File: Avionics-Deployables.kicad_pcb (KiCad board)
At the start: 2 copper layers, 82.6 x 90 mm, 0 parts

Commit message: Export BOM
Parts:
- added D1: DFLS130L-7, Diode_SMD:D_PowerDI-123, F.Cu at (109.4, 74.5)
- added D10: DFLS130L-7, Diode_SMD:D_PowerDI-123, B.Cu at (109.4, 117.0)
- added D2: DFLS130L-7, Diode_SMD:D_PowerDI-123, F.Cu at (109.4, 117.0)
- added D3: DFLS130L-7, Diode_SMD:D_PowerDI-123, F.Cu at (155.9, 129.8)
- added D4: DFLS130L-7, Diode_SMD:D_PowerDI-123, F.Cu at (185.3, 74.5)
- added D5: DFLS130L-7, Diode_SMD:D_PowerDI-123, F.Cu at (185.3, 117.0)
- added D6: DFLS130L-7, Diode_SMD:D_PowerDI-123, B.Cu at (185.3, 74.5)
- added D7: DFLS130L-7, Diode_SMD:D_PowerDI-123, B.Cu at (185.3, 117.0)
- added D8: DFLS130L-7, Diode_SMD:D_PowerDI-123, B.Cu at (138.7, 129.8)
- added D9: DFLS130L-7, Diode_SMD:D_PowerDI-123, B.Cu at (109.4, 74.5)
- added J1: 200528-0100, Connector_FFC-FPC:Molex_200528-0100_1x10-1MP_P1.00mm_Horizontal, B.Cu at (147.3, 136.2)
- added SC1: SM141K06TF, SolarPanels:SM141K06TF, F.Cu at (123.8, 74.5)
- added SC10: SM141K06TF, SolarPanels:SM141K06TF, B.Cu at (123.8, 117.0)
- added SC2: SM141K06TF, SolarPanels:SM141K06TF, F.Cu at (123.8, 117.0)
- added SC3: SM141K06TF, SolarPanels:SM141K06TF, F.Cu at (147.3, 106.7)
- added SC4: SM141K06TF, SolarPanels:SM141K06TF, F.Cu at (170.8, 74.5)
- added SC5: SM141K06TF, SolarPanels:SM141K06TF, F.Cu at (170.8, 117.0)
- added SC6: SM141K06TF, SolarPanels:SM141K06TF, B.Cu at (170.8, 74.5)
- added SC7: SM141K06TF, SolarPanels:SM141K06TF, B.Cu at (170.8, 117.0)
- added SC8: SM141K06TF, SolarPanels:SM141K06TF, B.Cu at (147.3, 106.7)
- added SC9: SM141K06TF, SolarPanels:SM141K06TF, B.Cu at (123.8, 74.5)
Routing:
- net Net-(D3-K): track 0.00 -> 130.5 mm
- net Net-(D8-K): track 0.00 -> 128.9 mm
- net Net-(D7-K): track 0.00 -> 77.3 mm
- net Net-(D2-K): track 0.00 -> 77.2 mm
- net Net-(D6-K): track 0.00 -> 63.2 mm
- net Net-(D4-K): track 0.00 -> 60.8 mm
- net Net-(D1-K): track 0.00 -> 60.8 mm
- net Net-(D10-A): track 0.00 -> 60.7 mm
- net D_VSOLAR1: track 0.00 -> 59.9 mm, vias 0 -> 3
- net D_VSOLAR2: track 0.00 -> 53.4 mm
- net GND: vias 0 -> 741
- added copper zone on B.Cu, net D_VSOLAR1
- added copper zone on B.Cu, net D_VSOLAR2
- added copper zone on B.Cu, net GND
- added copper zone on F.Cu, net GND
- removed copper zone on B.Cu, net (none)
- removed copper zone on F.Cu, net (none)
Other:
- outline, holes or cut-outs redrawn
- board text added: "1"
- board text added: "10"
- board text added: "ARGUS-1"
- board text added: "DVSOLAR1"
- board text added: "DVSOLAR2"
- board text added: "GND"
- board text added: "TO X/Y SOLAR PANEL"
- board text removed: "Solar Deployables Mechanical Stand-in 0.8mm"

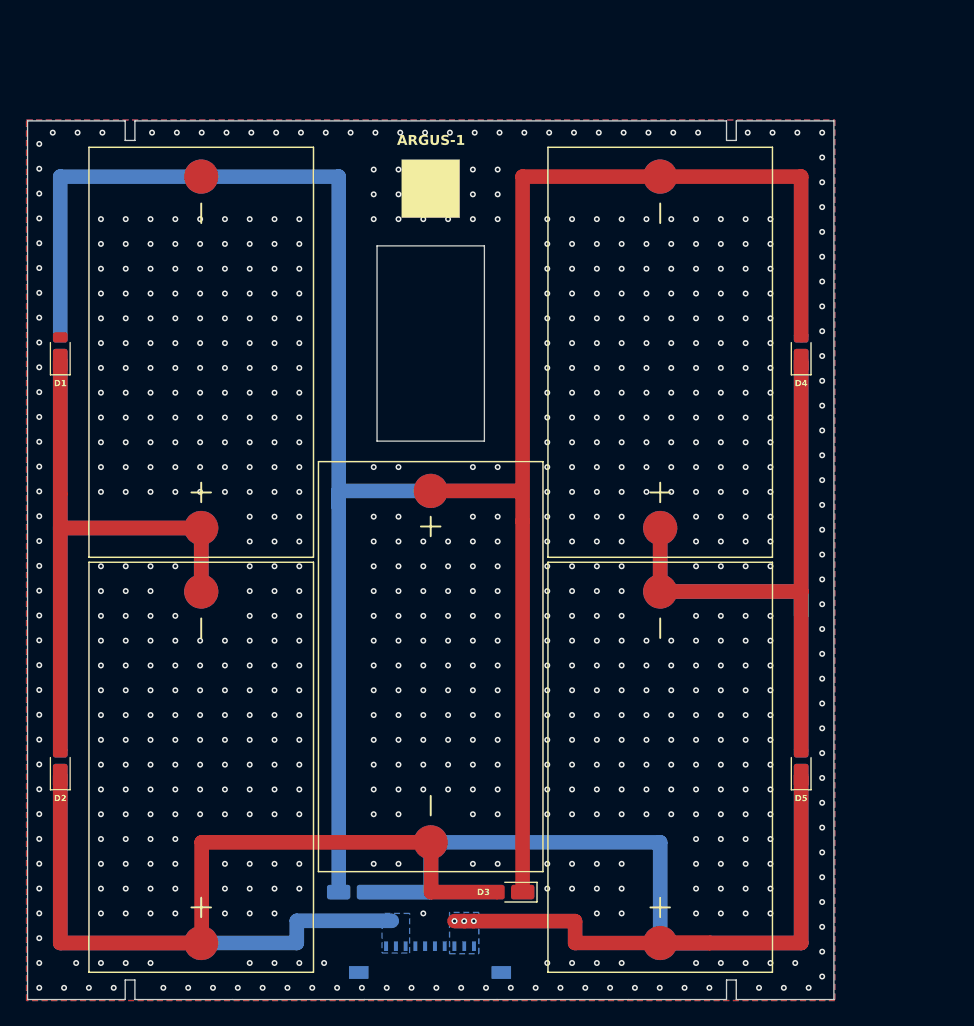
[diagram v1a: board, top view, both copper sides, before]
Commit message: Update Deployable outlines
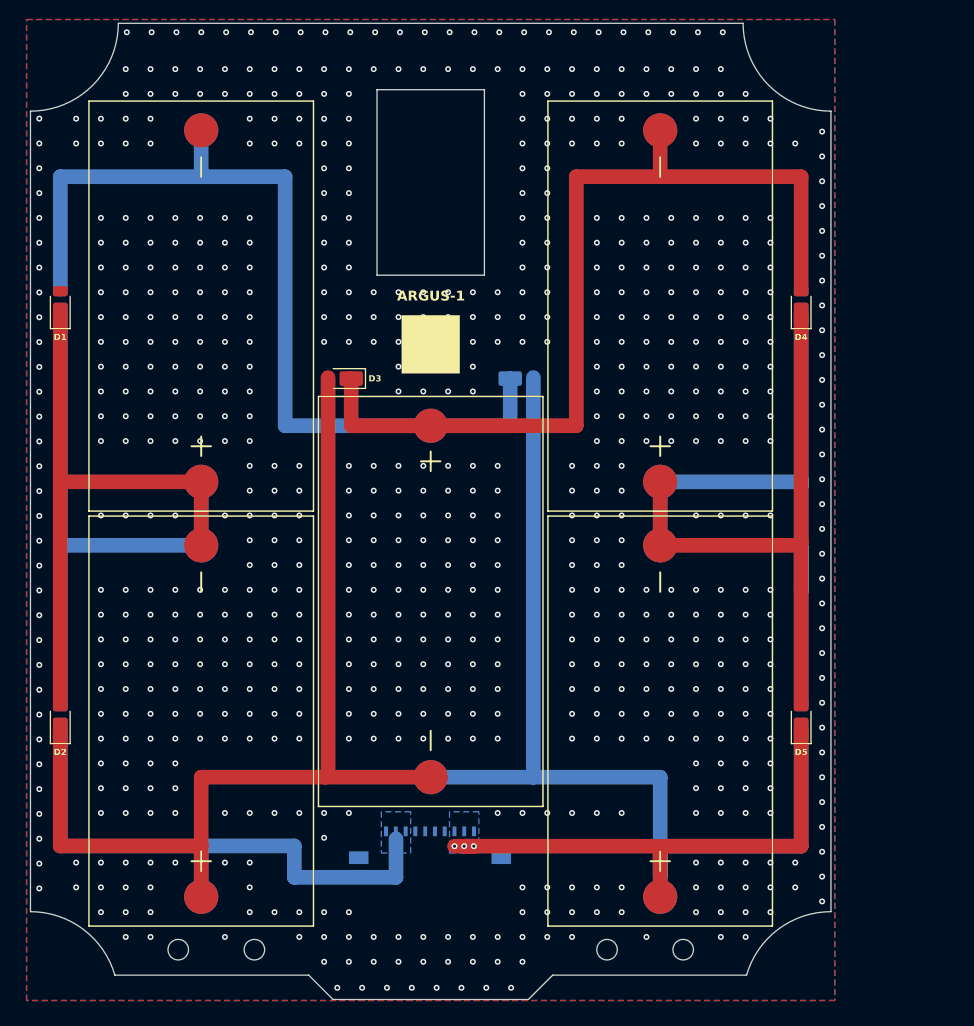
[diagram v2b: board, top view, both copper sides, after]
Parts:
- moved D3 55.5 mm to (138.3, 77.2)
- moved D8 55.5 mm to (156.3, 77.2)
- moved J1 11.8 mm to (147.3, 124.5)
- moved SC3 6.67 mm to (147.3, 100.0)
- moved SC8 6.67 mm to (147.3, 100.0)
- moved D10 4.73 mm to (109.4, 112.3)
- moved D2 4.73 mm to (109.4, 112.3)
- moved D5 4.73 mm to (185.3, 112.3)
- moved D7 4.73 mm to (185.3, 112.3)
- moved SC10 4.73 mm to (123.8, 112.3)
- moved SC2 4.73 mm to (123.8, 112.3)
- moved SC5 4.73 mm to (170.8, 112.3)
- moved SC7 4.73 mm to (170.8, 112.3)
- moved D1 4.73 mm to (109.4, 69.7)
- moved D4 4.73 mm to (185.3, 69.7)
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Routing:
- net Net-(D3-K): track 130.5 -> 92.7 mm
- net Net-(D8-K): track 128.9 -> 92.8 mm
- net Net-(D7-K): track 77.3 -> 106.2 mm
- net Net-(D2-K): track 77.2 -> 103.2 mm
- net D_VSOLAR1: track 59.9 -> 53.6 mm
- net D_VSOLAR2: track 53.4 -> 58.7 mm
- net Net-(D6-K): track 63.2 -> 66.2 mm
- net GND: vias 741 -> 744
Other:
- board size 82.6 x 90 mm -> 82 x 100 mm

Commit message: Update solar cell footprints
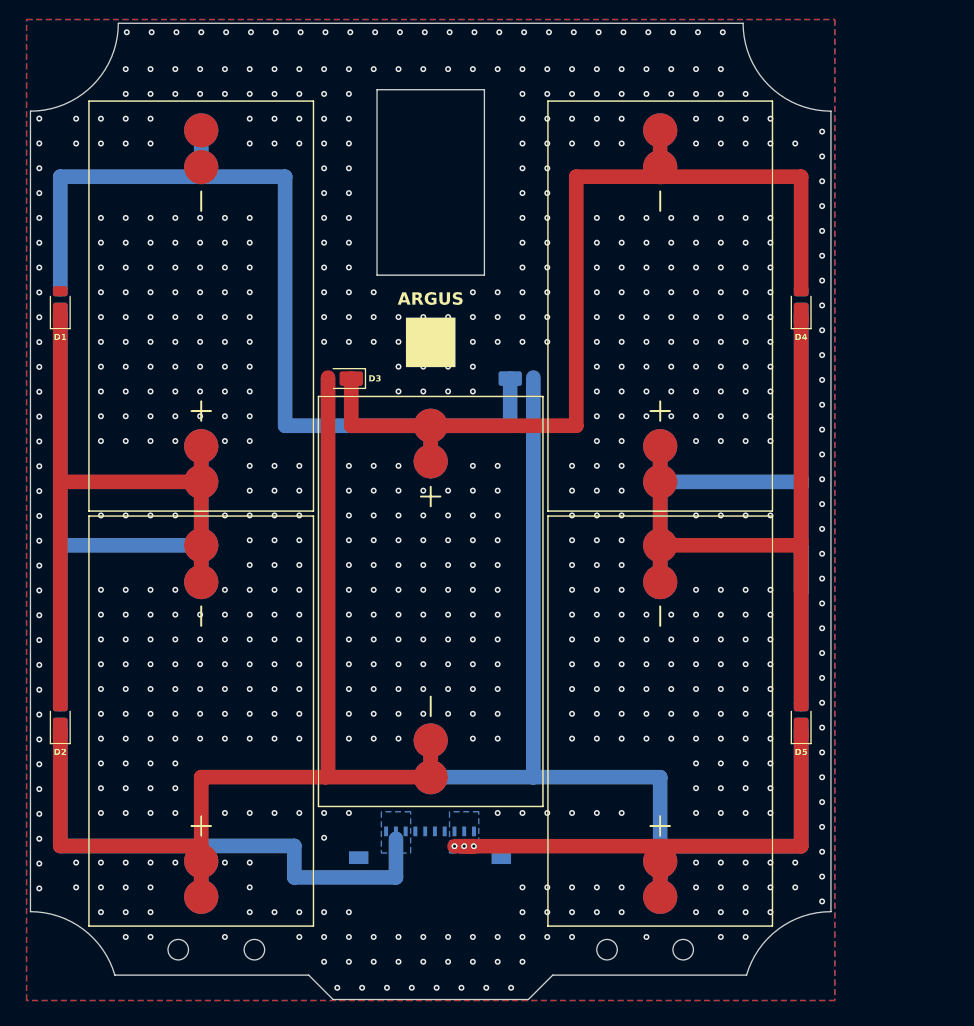
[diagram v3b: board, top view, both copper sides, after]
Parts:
- SC1, SC10, SC2, SC3, SC4, SC5, SC6, SC7, SC8, SC9: footprint SolarPanels:SM141K06TF -> SolarPanels:SM141K06TF-S
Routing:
- net Net-(D10-A): track 61.0 -> 68.4 mm
- net Net-(D4-K): track 61.0 -> 68.4 mm
- net Net-(D6-K): track 66.2 -> 73.6 mm
- net Net-(D1-K): track 60.9 -> 67.1 mm
- net Net-(D7-K): track 106.2 -> 109.9 mm
- net Net-(D2-K): track 103.2 -> 107.0 mm
- net Net-(D8-K): track 92.8 -> 96.4 mm
- net Net-(D3-K): track 92.7 -> 96.3 mm
- net GND: vias 744 -> 731
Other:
- board text added: "ARGUS"
- board text removed: "ARGUS-1"

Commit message: v2.3 Updates
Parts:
- added ?: , clipboard:eb50a26b-5fb6-463a-8dd0-ee5887daaa13, F.Cu at (142.4, 69.8)
- added ?: , clipboard:eb50a26b-5fb6-463a-8dd0-ee5887daaa13, B.Cu at (150.7, 69.8)
- added REF**: X Label, X Label, F.Cu at (146.6, 72.8)
- added REF**: X Label, X Label, B.Cu at (146.6, 72.8)
- added Ref**: Val**, custom-footprints:ypanel, F.Cu at (198.6, 73.1)
- added Ref**: Val**, custom-footprints:ypanel, B.Cu at (198.6, 73.1)
- SC1, SC10, SC2, SC3, SC4, SC5, SC6, SC7, SC8, SC9: value SM141K06TF -> SM141K06TF/S
- moved SC3 3.20 mm to (146.7, 103.1)
- moved SC8 3.20 mm to (146.7, 103.1)
- moved J1 1.76 mm to (146.6, 126.1)
- moved D3 1.71 mm to (136.9, 78.0), turned to 90 degrees
- moved D1 0.91 mm to (108.7, 70.4)
- moved D10 0.91 mm to (108.7, 112.9)
- moved D2 0.91 mm to (108.7, 112.9)
- moved D9 0.91 mm to (108.7, 70.4)
- moved D4 0.91 mm to (184.6, 70.4)
- moved D5 0.91 mm to (184.6, 112.9)
- moved D6 0.91 mm to (184.6, 70.4)
- moved D7 0.91 mm to (184.6, 112.9)
- moved SC1 0.91 mm to (123.2, 70.4)
- moved SC10 0.91 mm to (123.2, 112.9)
- moved SC2 0.91 mm to (123.2, 112.9)
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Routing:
- net D_VSOLAR2: track 58.7 -> 50.9 mm
- net Net-(D7-K): track 109.9 -> 115.8 mm
- net Net-(D8-K): track 96.4 -> 102.0 mm
- net Net-(D3-K): track 96.3 -> 101.9 mm
- net Net-(D2-K): track 107.0 -> 111.8 mm
- net D_VSOLAR1: track 53.6 -> 51.5 mm
- net GND: vias 731 -> 693
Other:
- outline, holes or cut-outs redrawn
- board text added: "ARGUS CUBESAT"
- board text removed: "ARGUS"

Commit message: V3 Updates and Cell Backer
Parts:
- added H1: MountingHole_Pad, TestPoint:TestPoint_Pad_D1.0mm, F.Cu at (109.6, 84.6)
- added H10: MountingHole_Pad, TestPoint:TestPoint_Pad_D1.0mm, B.Cu at (183.6, 84.6)
- added H11: MountingHole_Pad, TestPoint:TestPoint_Pad_D1.0mm, B.Cu at (183.6, 126.6)
- added H12: MountingHole_Pad, TestPoint:TestPoint_Pad_D1.0mm, B.Cu at (109.6, 56.6)
- added H13: MountingHole_Pad, TestPoint:TestPoint_Pad_D1.0mm, B.Cu at (109.6, 84.6)
- added H14: MountingHole_Pad, TestPoint:TestPoint_Pad_D1.0mm, B.Cu at (109.6, 126.6)
- added H15: MountingHole_Pad, TestPoint:TestPoint_Pad_D1.0mm, B.Cu at (183.6, 98.6)
- added H16: MountingHole_Pad, TestPoint:TestPoint_Pad_D1.0mm, B.Cu at (109.6, 98.6)
- added H17: MountingHole_Pad, TestPoint:TestPoint_Pad_D1.0mm, B.Cu at (183.6, 91.6)
- added H18: MountingHole_Pad, TestPoint:TestPoint_Pad_D1.0mm, B.Cu at (109.6, 91.6)
- added H19: MountingHole_Pad, TestPoint:TestPoint_Pad_D1.0mm, F.Cu at (183.6, 91.6)
- added H2: MountingHole_Pad, TestPoint:TestPoint_Pad_D1.0mm, F.Cu at (183.6, 84.6)
- added H20: MountingHole_Pad, TestPoint:TestPoint_Pad_D1.0mm, F.Cu at (109.6, 91.6)
- added H3: MountingHole_Pad, TestPoint:TestPoint_Pad_D1.0mm, F.Cu at (109.6, 56.6)
- added H4: MountingHole_Pad, TestPoint:TestPoint_Pad_D1.0mm, F.Cu at (109.6, 98.6)
- added H5: MountingHole_Pad, TestPoint:TestPoint_Pad_D1.0mm, F.Cu at (109.6, 126.6)
- added H6: MountingHole_Pad, TestPoint:TestPoint_Pad_D1.0mm, F.Cu at (183.6, 56.6)
- added H7: MountingHole_Pad, TestPoint:TestPoint_Pad_D1.0mm, F.Cu at (183.6, 98.6)
- added H8: MountingHole_Pad, TestPoint:TestPoint_Pad_D1.0mm, F.Cu at (183.6, 126.6)
- added H9: MountingHole_Pad, TestPoint:TestPoint_Pad_D1.0mm, B.Cu at (183.6, 56.6)
- D1, D10, D2, D3, D4, D5, D6, D7, D8, D9: value DFLS130L-7 -> DFLS130LQ-7
- SC1, SC10, SC2, SC3, SC4, SC5, SC6, SC7, SC8, SC9: footprint SolarPanels:SM141K06TF-S -> Argus-Miscellaneous:SM141K06TF_S
- moved D5 1.04 mm to (183.6, 112.6)
- moved D7 1.04 mm to (183.6, 112.6)
- moved D4 1.04 mm to (183.6, 70.6)
- moved D6 1.04 mm to (183.6, 70.6)
- moved D10 0.93 mm to (109.6, 112.6)
- moved D2 0.93 mm to (109.6, 112.6)
- moved D1 0.92 mm to (109.6, 70.6)
- moved D9 0.92 mm to (109.6, 70.6)
- moved SC5 0.62 mm to (169.6, 112.6)
- moved SC7 0.62 mm to (169.6, 112.6)
- moved SC4 0.62 mm to (169.6, 70.6)
- moved SC6 0.62 mm to (169.6, 70.6)
- moved SC10 0.52 mm to (123.6, 112.6)
- moved SC2 0.52 mm to (123.6, 112.6)
- moved SC1 0.51 mm to (123.6, 70.6)
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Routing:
- net Net-(D1-K): track 67.1 -> 75.1 mm
- net Net-(D4-K): track 68.4 -> 75.7 mm
- net Net-(D10-A): track 68.4 -> 75.5 mm
- net Net-(D2-K): track 111.8 -> 116.7 mm
- net Net-(D8-K): track 102.0 -> 106.2 mm
- net Net-(D6-K): track 73.6 -> 75.1 mm
- net D_VSOLAR2: track 50.9 -> 50.0 mm
- net Net-(D7-K): track 115.8 -> 115.2 mm
- net Net-(D3-K): track 101.9 -> 101.4 mm
- net GND: vias 693 -> 680
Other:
- outline, holes or cut-outs redrawn
